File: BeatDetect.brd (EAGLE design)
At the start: 31.4 x 23 mm, 24 parts, among them IC1 MCP602ST

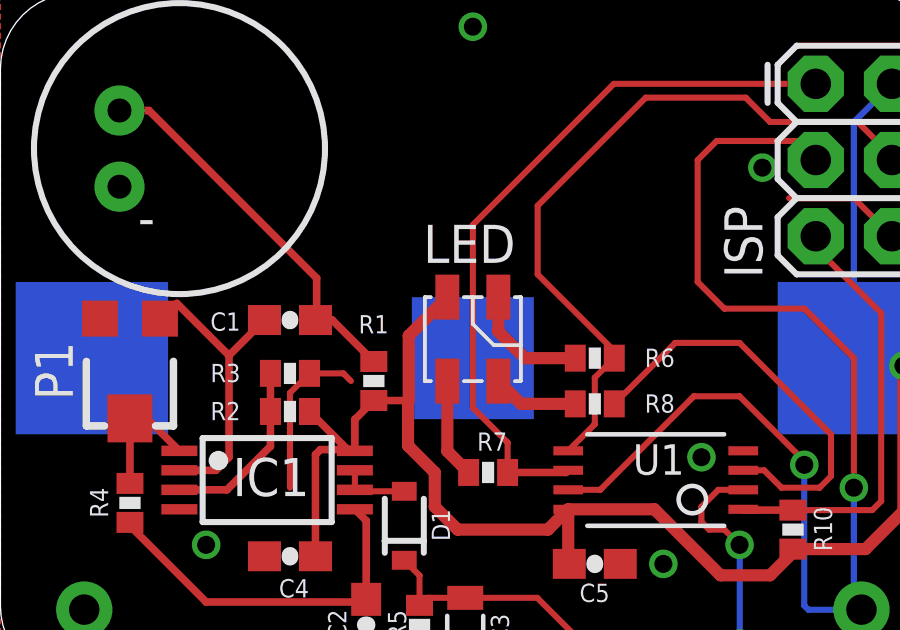
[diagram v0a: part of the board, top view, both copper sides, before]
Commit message: Fixing a bunch of small naming errors & part size mismatches.
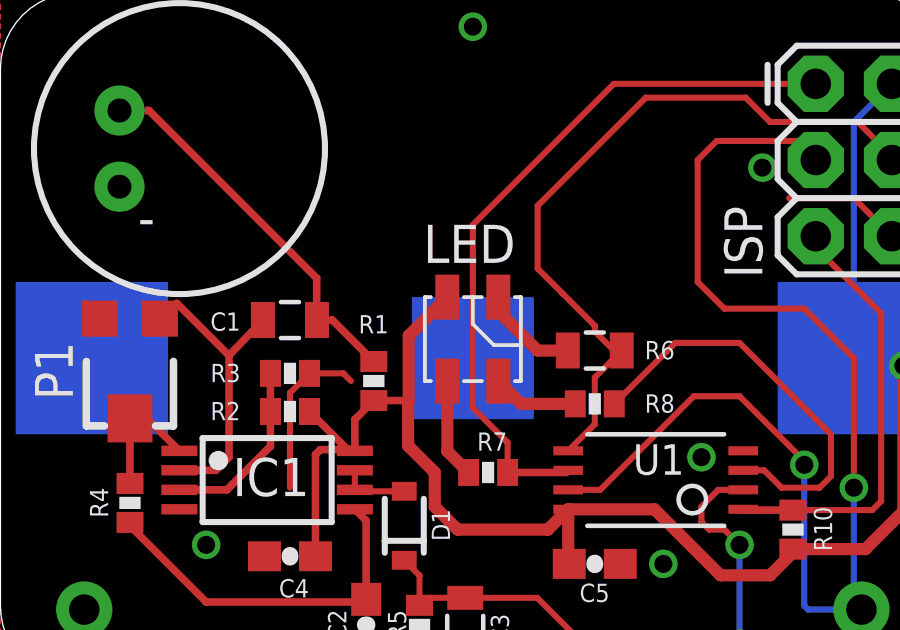
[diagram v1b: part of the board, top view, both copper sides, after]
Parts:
- C1: device SparkFun-Passives:0603-CAP -> SparkFun-Passives:0805
- C2: value 0.1uF -> .1uF
- R6: device SparkFun-Passives:0402-RES -> SparkFun-Passives:0805
- moved R6 0.25 mm to (19.8, 11.0)
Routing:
- net N$11: track 4.08 -> 3.33 mm
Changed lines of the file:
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@@
 <attribute name="NAME" x="2.9845" y="6.477" size="0.6096" layer="25" rot="R270"/>
 </element>
-<element name="C2" library="SparkFun-Passives" package="0603-CAP" value="0.1uF" x="12.192" y="1.905" smashed="yes" rot="R270">
+<element name="C2" library="SparkFun-Passives" package="0603-CAP" value=".1uF" x="12.192" y="1.905" smashed="yes" rot="R270">
 <attribute name="NAME" x="10.922" y="2.413" size="0.6096" layer="25" font="vector" ratio="12" rot="R270"/>
 </element>
@@
 <attribute name="NAME" x="11.938" y="11.6205" size="0.6096" layer="25"/>
 </element>
-<element name="C1" library="SparkFun-Passives" package="0603-CAP" value="1uF" x="9.652" y="12.065" smashed="yes" rot="R180">
+<element name="C1" library="SparkFun-Passives" package="0805" value="1uF" x="9.652" y="12.065" smashed="yes" rot="R180">
 <attribute name="NAME" x="8.001" y="12.319" size="0.6096" layer="25" font="vector" ratio="12" rot="R180"/>
 </element>
@@
 <attribute name="NAME" x="22.479" y="9.5885" size="0.6096" layer="25" rot="R180"/>
 </element>
-<element name="R6" library="SparkFun-Passives" package="0402-RES" value="75" x="19.812" y="10.795" smashed="yes" rot="R180">
-<attribute name="NAME" x="22.479" y="11.1125" size="0.6096" layer="25" rot="R180"/>
+<element name="R6" library="SparkFun-Passives" package="0805" value="75" x="19.812" y="11.049" smashed="yes" rot="R180">
+<attribute name="NAME" x="22.479" y="11.3665" size="0.6096" layer="25" rot="R180"/>
 </element>
 <element name="R7" library="SparkFun-Passives" package="0402-RES" value="20" x="16.256" y="6.985" smashed="yes" rot="R180">
@@
 <contactref element="C1" pad="1"/>
 <wire x1="12.446" y1="10.683" x2="11.064" y2="12.065" width="0.254" layer="1"/>
-<wire x1="11.064" y1="12.065" x2="10.502" y2="12.065" width="0.254" layer="1"/>
+<wire x1="11.064" y1="12.065" x2="10.552" y2="12.065" width="0.254" layer="1"/>
 <wire x1="10.541" y1="13.462" x2="10.541" y2="12.104" width="0.254" layer="1"/>
-<wire x1="10.541" y1="12.104" x2="10.502" y2="12.065" width="0.254" layer="1"/>
+<wire x1="10.541" y1="12.104" x2="10.552" y2="12.065" width="0.254" layer="1"/>
 <wire x1="10.541" y1="13.462" x2="4.953" y2="19.05" width="0.254" layer="1"/>
 <contactref element="U$2" pad="1"/>
@@
 <wire x1="7.183" y1="7.056" x2="7.62" y2="7.493" width="0.254" layer="1"/>
 <wire x1="7.62" y1="7.493" x2="7.62" y2="10.883" width="0.254" layer="1"/>
-<wire x1="7.62" y1="10.883" x2="8.802" y2="12.065" width="0.254" layer="1"/>
+<wire x1="7.62" y1="10.883" x2="8.752" y2="12.065" width="0.254" layer="1"/>
 <wire x1="7.62" y1="10.883" x2="5.883" y2="12.62" width="0.254" layer="1"/>
 <wire x1="5.883" y1="12.62" x2="5.318" y2="12.112" width="0.254" layer="1"/>
@@
 <contactref element="ISP" pad="4"/>
 <wire x1="18.9262" y1="7.706" x2="19.812" y2="8.5918" width="0.2032" layer="1"/>
-<wire x1="19.812" y1="8.5918" x2="19.812" y2="10.145" width="0.2032" layer="1"/>
-<wire x1="19.812" y1="10.145" x2="20.462" y2="10.795" width="0.2032" layer="1"/>
+<wire x1="19.812" y1="8.5918" x2="19.812" y2="10.149" width="0.2032" layer="1"/>
 <wire x1="25.654" y1="18.669" x2="28.575" y2="18.669" width="0.2032" layer="1"/>
 <wire x1="28.575" y1="18.669" x2="29.718" y2="17.526" width="0.2032" layer="1"/>
@@
 <wire x1="24.8443" y1="19.4787" x2="25.654" y2="18.669" width="0.2032" layer="1"/>
 <wire x1="21.5107" y1="19.4787" x2="17.907" y2="15.875" width="0.2032" layer="1"/>
-<wire x1="17.907" y1="15.875" x2="17.907" y2="13.589" width="0.2032" layer="1"/>
-<wire x1="17.907" y1="13.589" x2="20.462" y2="11.034" width="0.2032" layer="1"/>
-<wire x1="20.462" y1="11.034" x2="20.462" y2="10.795" width="0.2032" layer="1"/>
+<wire x1="18.734371875" y1="12.954" x2="17.907" y2="13.781371875" width="0.2032" layer="1"/>
+<wire x1="17.907" y1="13.781371875" x2="17.907" y2="15.875" width="0.2032" layer="1"/>
+<wire x1="20.462" y1="11.034" x2="20.712" y2="11.049" width="0.2032" layer="1"/>
+<wire x1="19.812" y1="10.149" x2="20.712" y2="11.049" width="0.2032" layer="1"/>
+<wire x1="20.462" y1="11.034" x2="19.812" y2="11.684" width="0.2032" layer="1"/>
+<wire x1="19.812" y1="11.684" x2="19.812" y2="11.876371875" width="0.2032" layer="1"/>
+<wire x1="19.812" y1="11.876371875" x2="18.734371875" y2="12.954" width="0.2032" layer="1"/>
 </signal>
 <signal name="N$9">
@@
 <contactref element="LED" pad="R"/>
 <contactref element="R6" pad="2"/>
-<wire x1="17.49" y1="10.795" x2="19.162" y2="10.795" width="0.4064" layer="1"/>
-<wire x1="16.598" y1="12.83" x2="16.598" y2="11.687" width="0.4064" layer="1"/>
-<wire x1="16.598" y1="11.687" x2="17.49" y2="10.795" width="0.4064" layer="1"/>
+<wire x1="18.912" y1="11.049" x2="17.907" y2="11.049" width="0.4064" layer="1"/>
+<wire x1="17.907" y1="11.049" x2="16.598" y2="12.358" width="0.4064" layer="1"/>
+<wire x1="16.598" y1="12.358" x2="16.598" y2="12.83" width="0.4064" layer="1"/>
 </signal>
 <signal name="N$12">

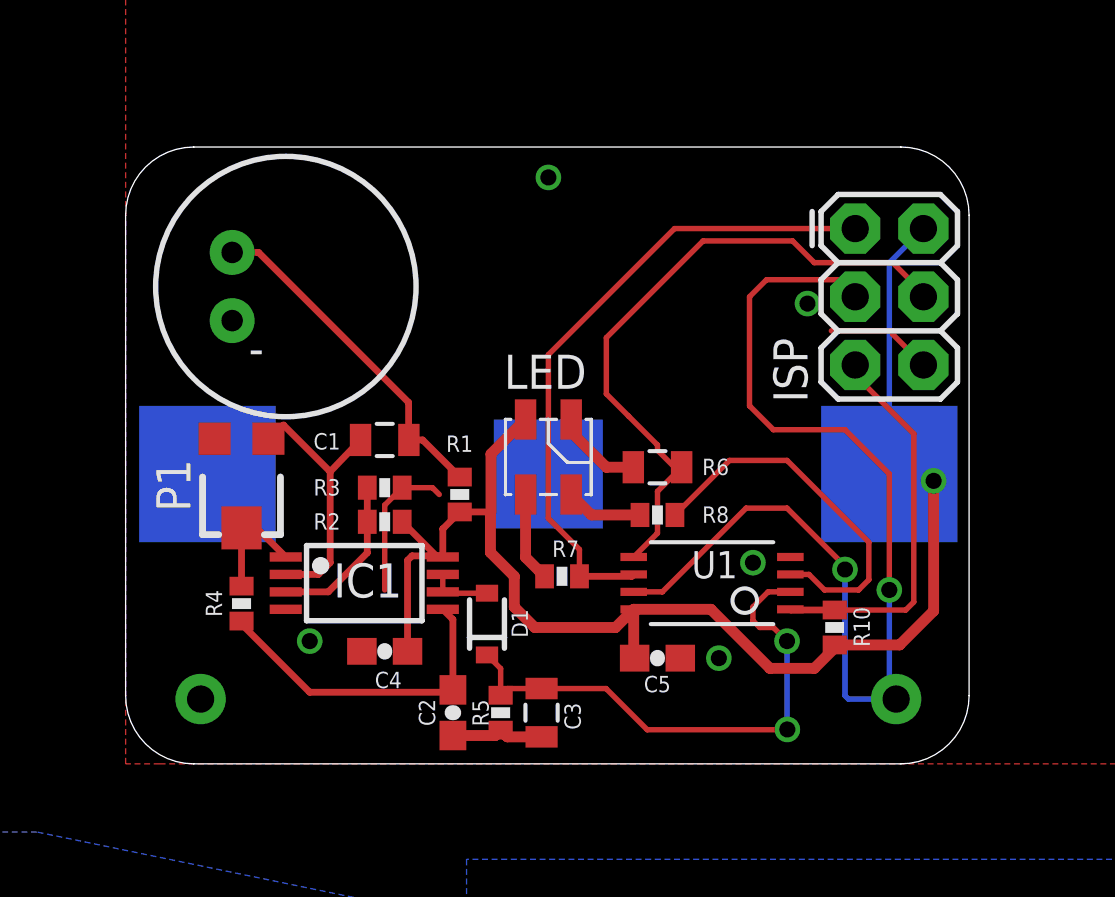
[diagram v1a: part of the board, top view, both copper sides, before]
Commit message: Added power diode to isolate LED supply from MCU & etc. supply.
Makes it a lot easier to safely program the MCU w/o turning the LED on
and prevents backfriving current into the battery.
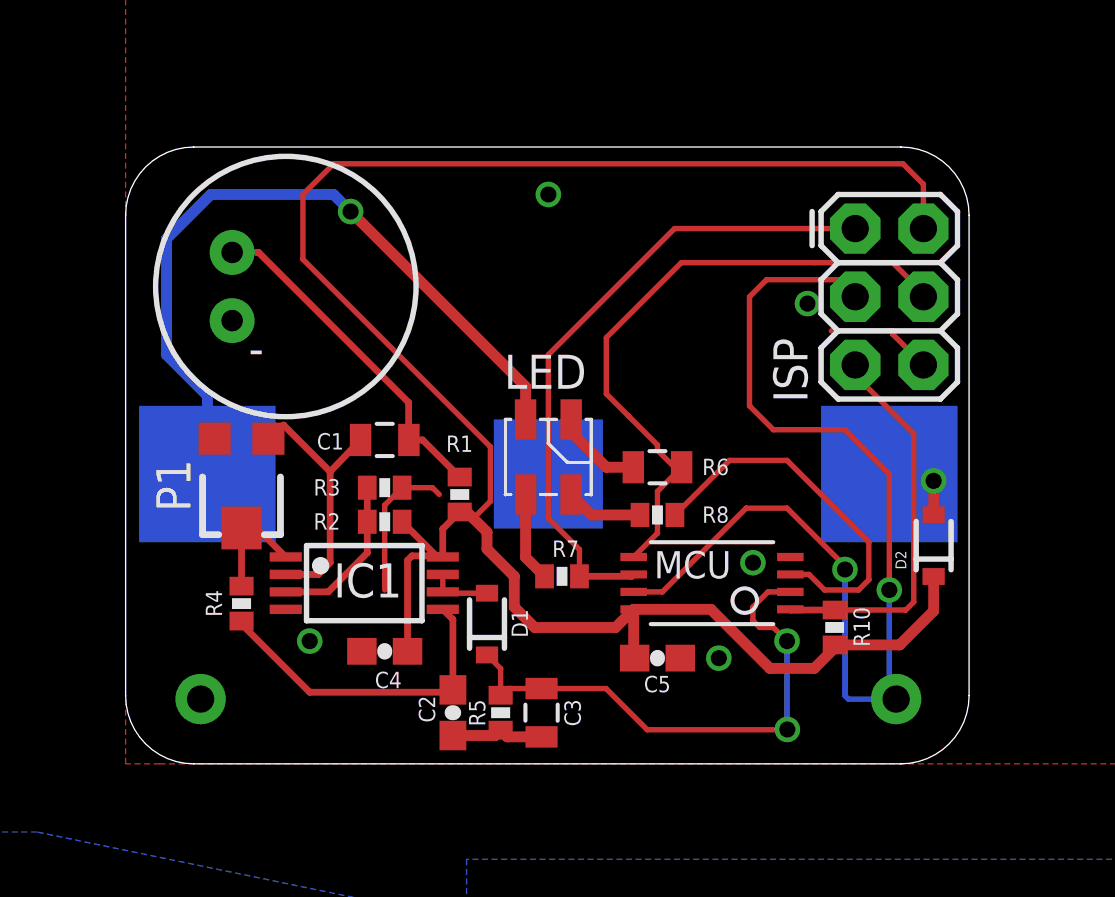
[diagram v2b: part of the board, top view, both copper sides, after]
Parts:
- added D2: (no value), SparkFun-DiscreteSemi:SOD-323
- renumbered U1 to MCU
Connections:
- new net N$7: D2.2, U$1.+$2
- new net VBATT: LED.A, U$1.+$1
- net VCC: now also D2.1; no longer LED.A, U$1.+$2
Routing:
- net VBATT: track 0.00 -> 27.6 mm, vias 0 -> 1
- net VCC: track 54.0 -> 75.3 mm, vias 1 -> 0
- net N$7: track 0.00 -> 3.33 mm, vias 0 -> 1
- net MOSI: track 24.5 -> 23.8 mm
